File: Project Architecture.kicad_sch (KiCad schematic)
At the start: 0 parts

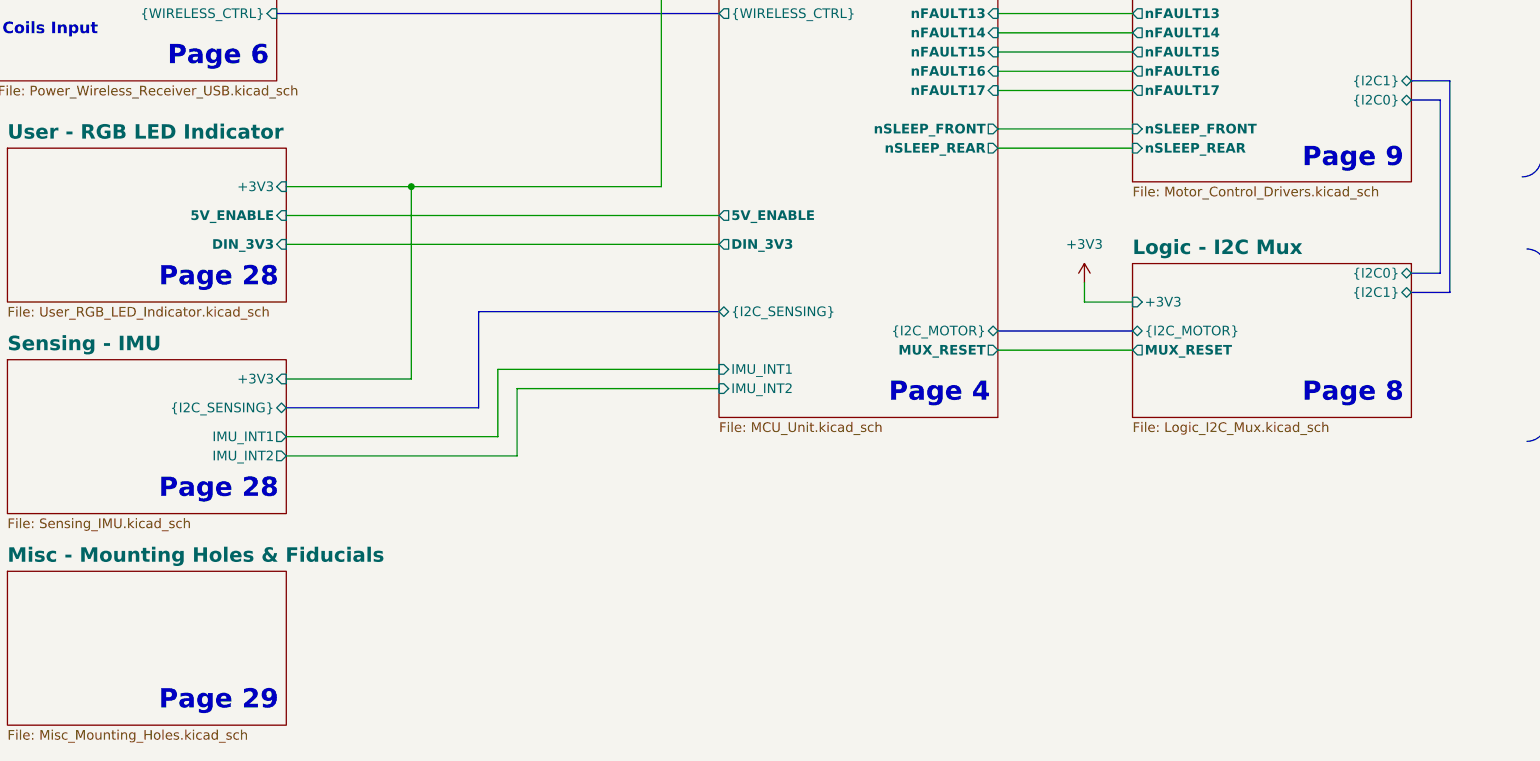
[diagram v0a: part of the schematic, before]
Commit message: Finished cleaning routing, removed errors, cleaned shematics, added pictures and other improvements
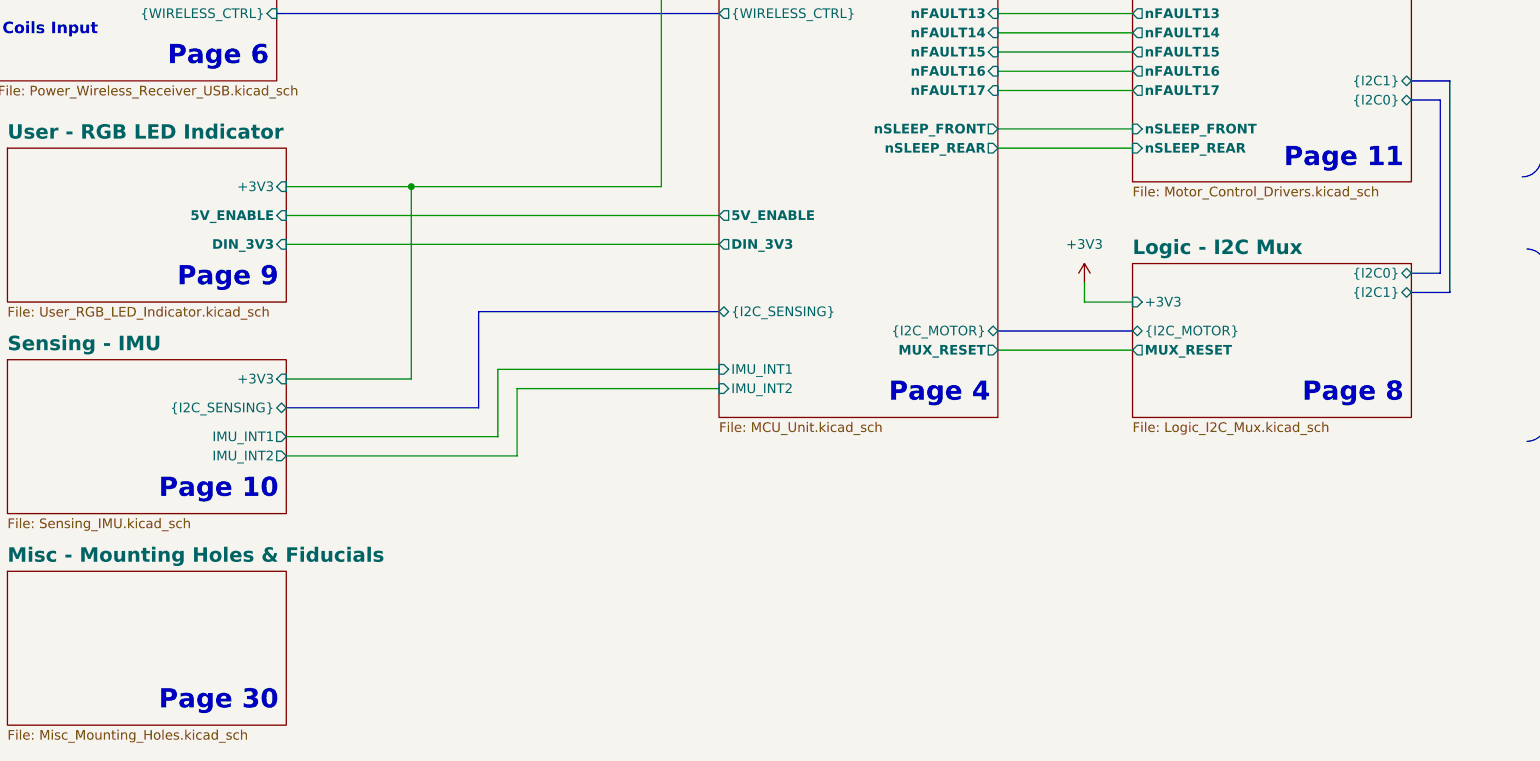
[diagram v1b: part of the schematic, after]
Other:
- note added: "Page 10"
- note added: "Page 11"
- note added: "Page 30"
- note removed: "Page 28"
- note removed: "Page 29"
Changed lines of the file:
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@@
 		)
 	)
-	(text "Page 28"
+	(text "Page 10"
 		(exclude_from_sim no)
 		(at 87.884 156.972 0)
@@
 				(size 2.54 2.54)
 				(bold yes)
-				(color 20 60 40 1)
+				(color 0 0 0 1)
 			)
 			(justify right bottom)
-			(href "#28")
-		)
-	)
-	(text "Page 28"
+			(href "#10")
+		)
+	)
+	(text "Page 9"
 		(exclude_from_sim no)
 		(at 87.884 129.032 0)
@@
 				(size 2.54 2.54)
 				(bold yes)
-				(color 20 60 40 1)
+				(color 0 0 0 1)
 			)
 			(justify right bottom)
-			(href "#28")
+			(href "#9")
 		)
 	)
@@
 		)
 	)
-	(text "Page 9"
+	(text "Page 11"
 		(exclude_from_sim no)
 		(at 236.474 113.284 0)
@@
 			)
 			(justify right bottom)
-			(href "#9")
+			(href "#11")
 		)
 	)
@@
 		)
 	)
-	(text "Page 29"
+	(text "Page 30"
 		(exclude_from_sim no)
 		(at 87.884 184.912 0)
@@
 				(size 2.54 2.54)
 				(bold yes)
-				(color 20 60 40 1)
+				(color 0 0 0 1)
 			)
 			(justify right bottom)
-			(href "#29")
+			(href "#30")
 		)
 	)
@@
 				(font
 					(size 1.27 1.27)
+					(color 0 0 0 1)
 				)
 				(justify right)
@@
 				(font
 					(size 1.27 1.27)
+					(color 0 0 0 1)
 				)
 				(justify right)
@@
 			(project "Plume"
 				(path "/0650c7a8-acba-429c-9f8e-eec0baf0bc1c/fede4c36-00cc-4d3d-b71c-5243ba232202"
-					(page "32")
+					(page "10")
 				)
 			)
@@
 			(project "Plume"
 				(path "/0650c7a8-acba-429c-9f8e-eec0baf0bc1c/fede4c36-00cc-4d3d-b71c-5243ba232202"
-					(page "9")
+					(page "11")
 				)
 			)
@@
 			(project "Plume"
 				(path "/0650c7a8-acba-429c-9f8e-eec0baf0bc1c/fede4c36-00cc-4d3d-b71c-5243ba232202"
-					(page "28")
+					(page "9")
 				)
 			)
@@
 				(font
 					(size 1.27 1.27)
+					(color 0 0 0 1)
 				)
 				(justify left)
@@
 				(font
 					(size 1.27 1.27)
+					(color 0 0 0 1)
 				)
 				(justify left)
@@
 			(project "Plume"
 				(path "/0650c7a8-acba-429c-9f8e-eec0baf0bc1c/fede4c36-00cc-4d3d-b71c-5243ba232202"
-					(page "29")
-				)
-			)
+					(page "30")
+				)
+			)
